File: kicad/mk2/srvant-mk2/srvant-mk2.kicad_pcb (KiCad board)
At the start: 2 copper layers, 172 parts, among them J2 Bus_M.2_Socket_M, J4 ARJM11, J5 ARJM11, U1 INA219AxDCN, U10 RT9742SNGV, U11 BSZ040N04LSGATMA1, U13 KSZ9131RNXI-TR, U14 TPD4EUSB30, U15 TPD4EUSB30, U2 AP64501SP-13, U5 PCF85063AT/AAZ, U6 74LVC1G07SE-7, U7 74LVC1G07SE-7, U8 TPD4EUSB30, U9 TPD4EUSB30, Y1 X32K768S301

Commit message: more progress
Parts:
- removed C30, C31: 100n, Capacitor_SMD:C_0402_1005Metric
- removed R8: 100K/1%, Resistor_SMD:R_0402_1005Metric
- removed U11: BSZ040N04LSGATMA1, footprints:bsz086p03ns
- removed U12: ~, rp-t113-s3:rp-t113-s3
- added C76: 100n, Capacitor_SMD:C_0402_1005Metric, F.Cu at (38.9, 121.3)
- added FB7: 220R, Resistor_SMD:R_0402_1005Metric, F.Cu at (38.9, 119.3)
- added J1: Barrel_Jack_Switch, footprints:DC-jack-694106301002, F.Cu at (153.2, 82.0)
- added J3: HDMI connector, footprints:HDMI-10029449-001RLF, F.Cu at (148.3, 68.8)
- added Q1: DMP3013SFV-7, Package_SON:Diodes_PowerDI3333-8, F.Cu at (141.4, 90.7)
- added R1: 12K, Resistor_SMD:R_0402_1005Metric, F.Cu at (148.5, 89.3)
- added R15: 3.3K, Resistor_SMD:R_0402_1005Metric, F.Cu at (34.0, 119.3)
- added R16: 3.3K, Resistor_SMD:R_0402_1005Metric, F.Cu at (34.0, 121.3)
- added R17: 10R, Resistor_SMD:R_0402_1005Metric, F.Cu at (34.0, 123.3)
- added R18: 10R, Resistor_SMD:R_0402_1005Metric, F.Cu at (34.0, 125.3)
- added TP1: TestPoint (VIN), TestPoint:TestPoint_Pad_D1.0mm, F.Cu at (145.5, 89.8)
- added U3: TLV62585DRLR, TLV62585DRLR:DRL0006A, F.Cu at (43.9, 119.9)
- added U4: rp-t113-s3, rp-t113-s3:rp-t113-s3, F.Cu at (12.8, 38.6)
- added Y2: 25Mhz, footprints:LFXTAL-25MHz, F.Cu at (161.9, 80.0)
- TP8: footprint TestPoint:TestPoint_Pad_2.0x2.0mm -> TestPoint:TestPoint_Pad_D1.0mm
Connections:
- J4 pad SH: GND -> Net-(FB7-Pad1)
- TP8 pad 1: Net-(D2-K) -> /bmc/PHY_DVDDH
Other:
- board outline added: 5.8 x 5.9 mm

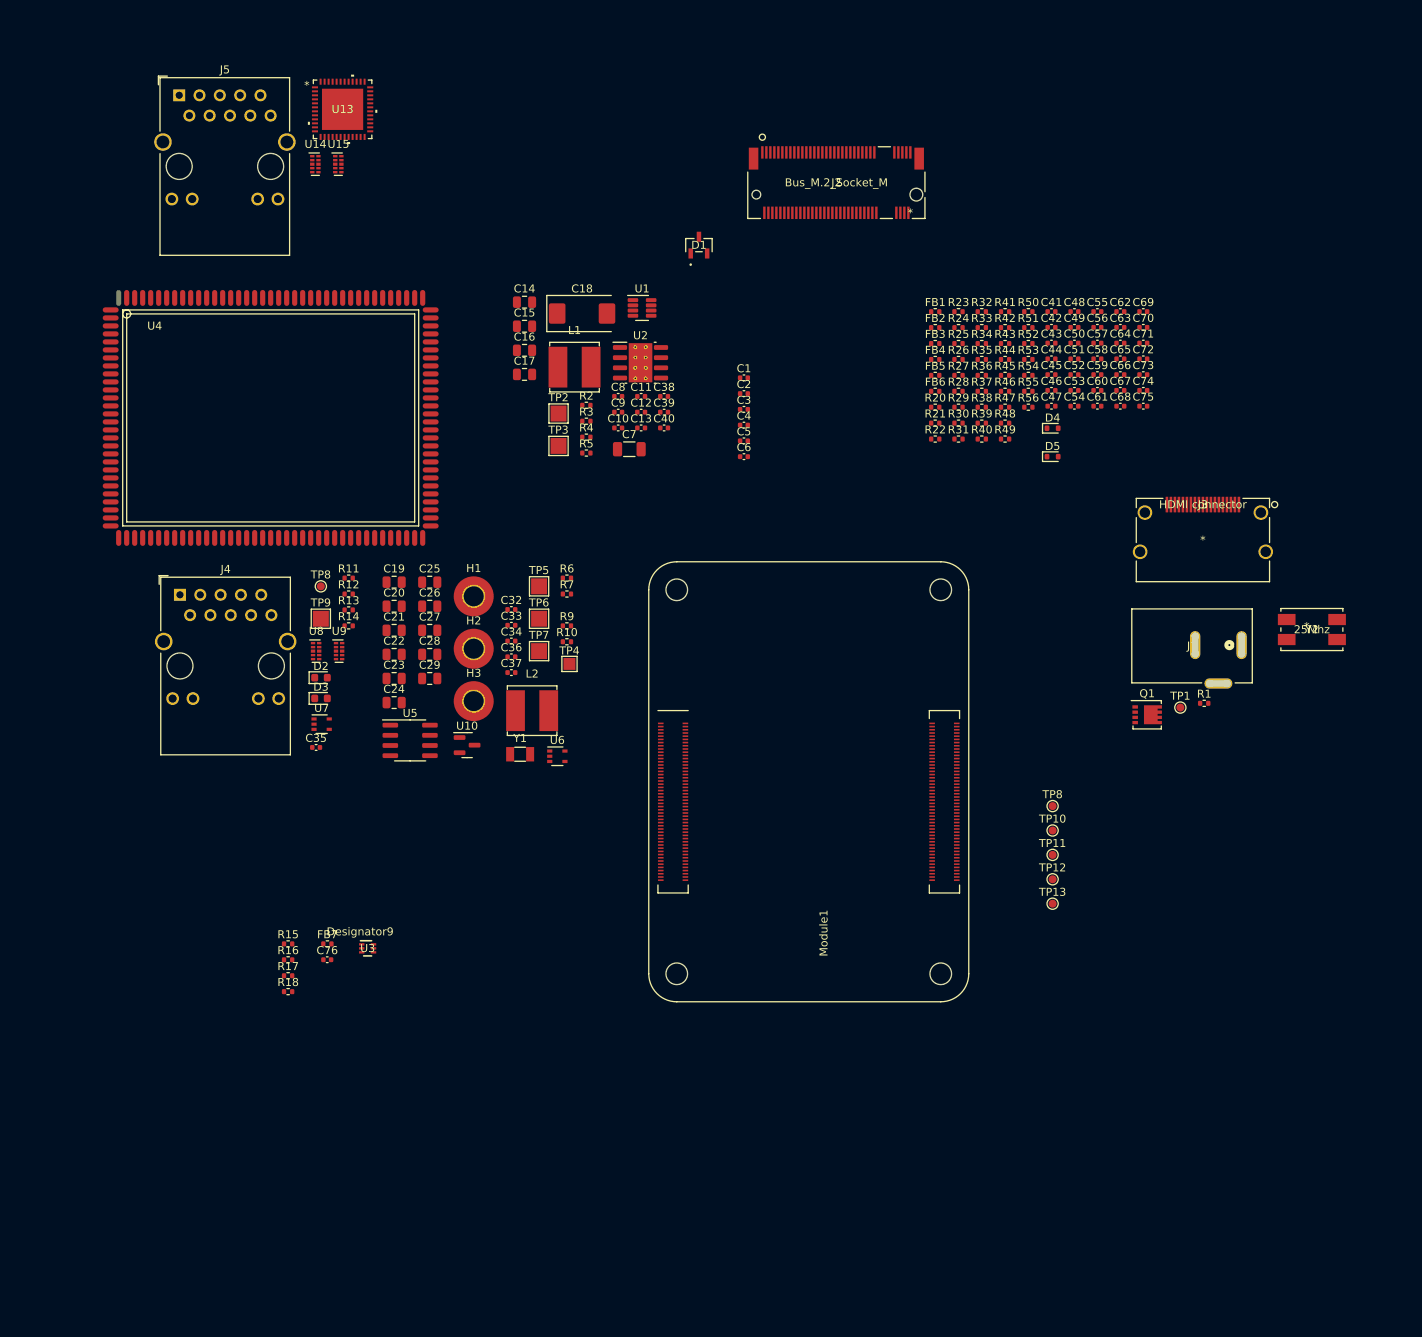
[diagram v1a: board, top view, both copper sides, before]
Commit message: merge cm4 into one page, basic interconnection
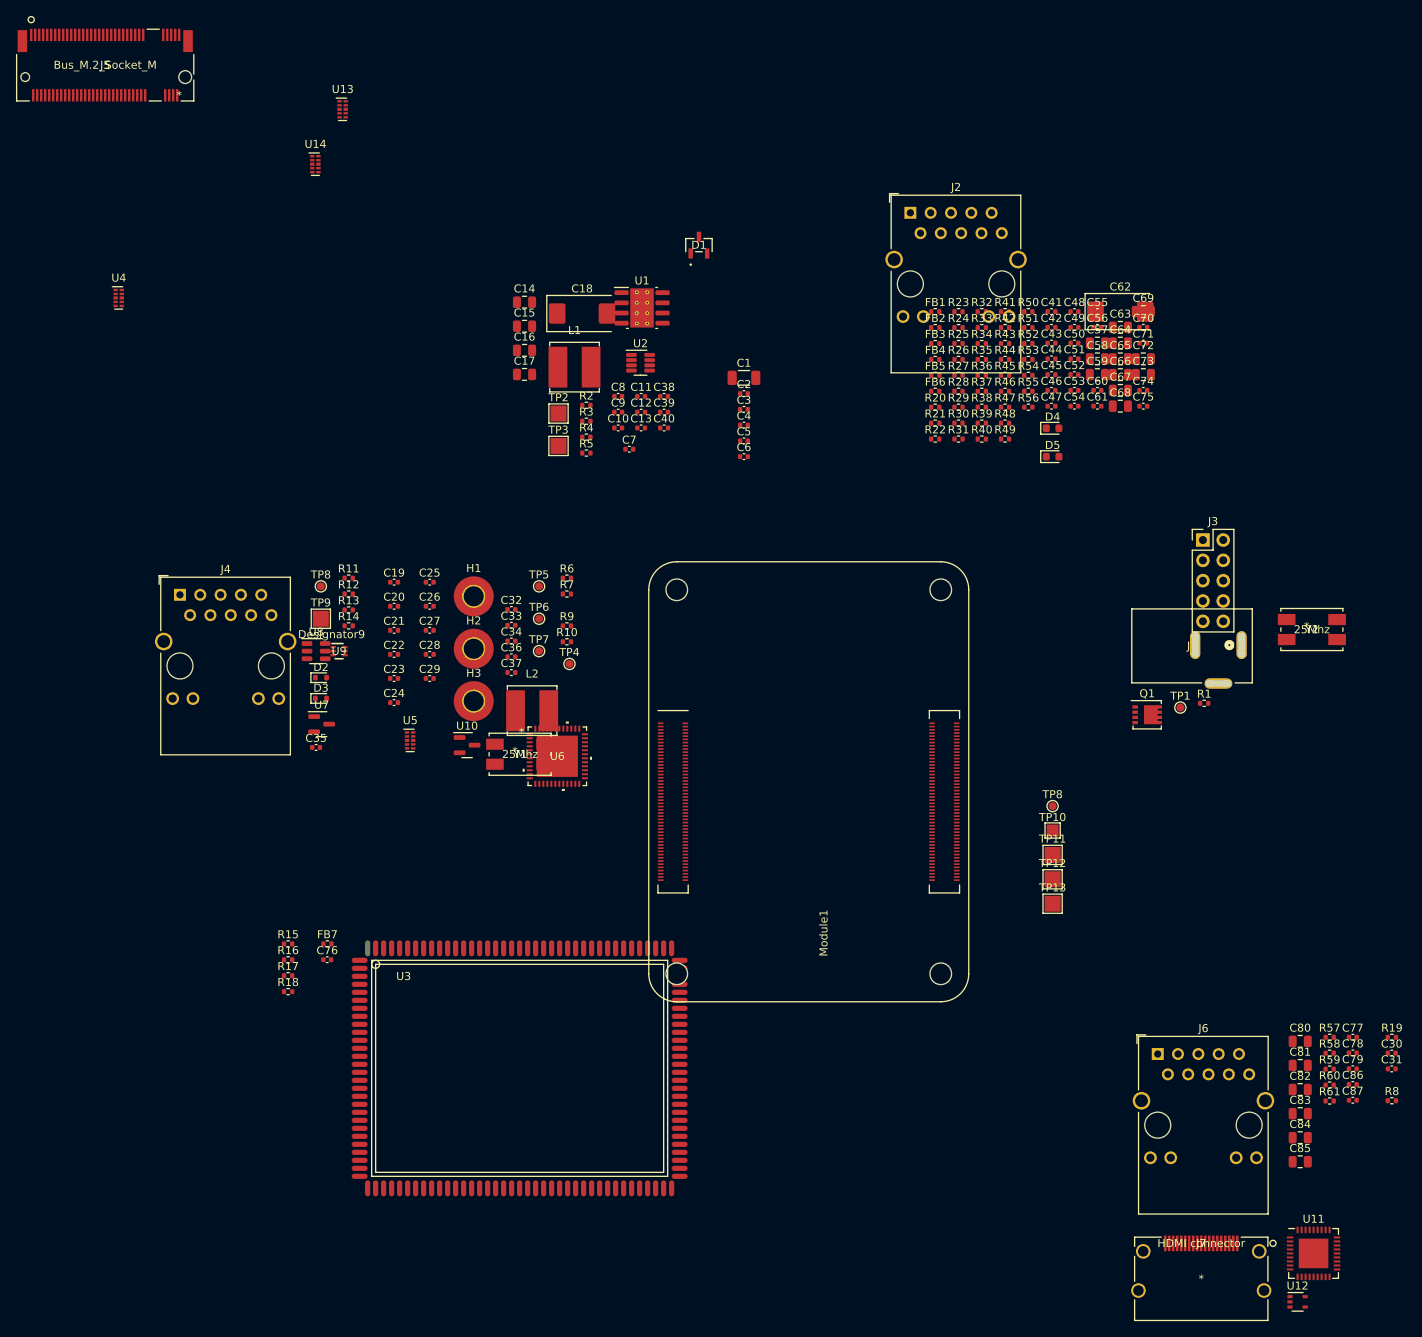
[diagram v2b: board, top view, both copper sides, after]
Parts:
- removed U15: TPD4EUSB30, Package_SON:USON-10_2.5x1.0mm_P0.5mm
- added C30: 100n, Capacitor_SMD:C_0402_1005Metric, F.Cu at (171.9, 133.0)
- added C31: 100n, Capacitor_SMD:C_0402_1005Metric, F.Cu at (171.9, 134.9)
- added C77: 100n, Capacitor_SMD:C_0402_1005Metric, F.Cu at (167.1, 131.0)
- added C78: 100n, Capacitor_SMD:C_0402_1005Metric, F.Cu at (167.1, 133.0)
- added C79: 100n, Capacitor_SMD:C_0402_1005Metric, F.Cu at (167.1, 134.9)
- added C80: 10u, Capacitor_SMD:C_0805_2012Metric, F.Cu at (160.5, 131.5)
- added C81: 10u, Capacitor_SMD:C_0805_2012Metric, F.Cu at (160.5, 134.5)
- added C82: 10u, Capacitor_SMD:C_0805_2012Metric, F.Cu at (160.5, 137.5)
- added C83: 100n, Capacitor_SMD:C_0805_2012Metric, F.Cu at (160.5, 140.5)
- added C84: 100n, Capacitor_SMD:C_0805_2012Metric, F.Cu at (160.5, 143.6)
- added C85: 100n, Capacitor_SMD:C_0805_2012Metric, F.Cu at (160.5, 146.6)
- added C86: 100n, Capacitor_SMD:C_0402_1005Metric, F.Cu at (167.1, 136.9)
- added C87: 100n, Capacitor_SMD:C_0402_1005Metric, F.Cu at (167.1, 138.9)
- added J6: ARJM11, Connector_RJ:RJ45_Wuerth_7499111446_Horizontal, F.Cu at (142.7, 133.1)
- added J7: HDMI connector, footprints:HDMI-10029449-001RLF, F.Cu at (148.1, 161.2)
- added R19: 10K, Resistor_SMD:R_0402_1005Metric, F.Cu at (172.0, 131.0)
- added R57: 12K/1%, Resistor_SMD:R_0402_1005Metric, F.Cu at (164.2, 131.0)
- added R58: 36K/1%, Resistor_SMD:R_0402_1005Metric, F.Cu at (164.2, 133.0)
- added R59: 1K, Resistor_SMD:R_0402_1005Metric, F.Cu at (164.2, 135.0)
- added R60: 470R, Resistor_SMD:R_0402_1005Metric, F.Cu at (164.2, 137.0)
- added R61: 470R, Resistor_SMD:R_0402_1005Metric, F.Cu at (164.2, 139.0)
- added R8: 10R, Resistor_SMD:R_0402_1005Metric, F.Cu at (172.0, 138.9)
- added U11: USB2514B-I/M2, Package_DFN_QFN:QFN-36-1EP_6x6mm_P0.5mm_EP3.7x3.7mm, F.Cu at (162.2, 158.0)
- added U12: 74LVC1G07SE-7, Package_TO_SOT_SMD:SOT-353_SC-70-5, F.Cu at (160.2, 164.1)
- C1: value 10u/35v -> 100n/100v; footprint Capacitor_SMD:C_0402_1005Metric -> Capacitor_SMD:C_1206_3216Metric
- C19: value 10u 35v -> 100n; footprint Capacitor_SMD:C_0805_2012Metric -> Capacitor_SMD:C_0402_1005Metric
- C2, C39, C75: value 10u/35v -> 100n
- C20: value 10u 35v -> 10u/35v; footprint Capacitor_SMD:C_0805_2012Metric -> Capacitor_SMD:C_0402_1005Metric
- C21, C24, C25, C26, C28: value 10u -> 100n; footprint Capacitor_SMD:C_0805_2012Metric -> Capacitor_SMD:C_0402_1005Metric
- C22: value 10u -> 10u/35v; footprint Capacitor_SMD:C_0805_2012Metric -> Capacitor_SMD:C_0402_1005Metric
- C23, C27, C29: footprint Capacitor_SMD:C_0805_2012Metric -> Capacitor_SMD:C_0402_1005Metric
- C37, C41, C42, C43, C44, C8, C9: value 100n -> 10u/35v
- C55, C56: value 100n -> 15p
- C57, C59: value 100n -> 10u 35v; footprint Capacitor_SMD:C_0402_1005Metric -> Capacitor_SMD:C_0805_2012Metric
- C58, C63, C69: value 100n -> 10u; footprint Capacitor_SMD:C_0402_1005Metric -> Capacitor_SMD:C_0805_2012Metric
- C62: value 100n -> 100u; footprint Capacitor_SMD:C_0402_1005Metric -> Capacitor_Tantalum_SMD:CP_EIA-7343-31_Kemet-D
- C64, C65, C66, C67, C68, C73: value 10u/35v -> 10u; footprint Capacitor_SMD:C_0402_1005Metric -> Capacitor_SMD:C_0805_2012Metric
- C7: value 100n/100v -> 10u/35v; footprint Capacitor_SMD:C_1206_3216Metric -> Capacitor_SMD:C_0402_1005Metric
- C70: value 100n -> 27p
- C71: value 15p -> 27p
- C72: value 15p -> 10u; footprint Capacitor_SMD:C_0402_1005Metric -> Capacitor_SMD:C_0805_2012Metric
- D2: value LED Green -> 1N4148; footprint LED_SMD:LED_0603_1608Metric -> Diode_SMD:D_SOD-523
- D3: value LED Red -> 1N4148; footprint LED_SMD:LED_0603_1608Metric -> Diode_SMD:D_SOD-523
- D4: value 1N4148 -> LED Green; footprint Diode_SMD:D_SOD-523 -> LED_SMD:LED_0603_1608Metric
- D5: value 1N4148 -> LED Red; footprint Diode_SMD:D_SOD-523 -> LED_SMD:LED_0603_1608Metric
- J2: value Bus_M.2_Socket_M -> ARJM11; footprint footprints:1-2199230-5 -> Connector_RJ:RJ45_Wuerth_7499111446_Horizontal
- J3: value HDMI connector -> Conn_02x05_Odd_Even; footprint footprints:HDMI-10029449-001RLF -> Connector_PinHeader_2.54mm:PinHeader_2x05_P2.54mm_Vertical
- J5: value ARJM11 -> Bus_M.2_Socket_M; footprint Connector_RJ:RJ45_Wuerth_7499111446_Horizontal -> footprints:1-2199230-5
- R10, R9: value 510K/1% -> 3.3K
- R11, R12: value 1K -> 330R
- R13, R14: value 470R -> 22R
- R15, R16: value 3.3K -> 22R
- R17, R18: value 10R -> 22R
- R2: value 20K 1% -> 10R
- R20: value 330R -> 10K
- R21: value 330R -> 1K
- R24: value 10K -> 6.04K
- R25: value 6.04K -> 10K
- R26, R28, R30: value 22R -> 1K
- R27, R29, R37: value 22R -> 10K
- R3: value 12K 1% -> 20K 1%
- R38, R40, R47, R54: value 10K -> 1K
- R4: value 2.2K 1% -> 12K 1%
- R44, R46: value 1K -> 10K
- R48: value 1K -> 15K/1%
- R49: value 10K -> 100K 1%
- R5: value 10R -> 2.2K 1%
- R50: value 1K -> 22K 1%
- R51: value 10K -> 2.2K/1%
- R52: value 1K -> 2.2K/1%
- R53, R55: value 1K -> 36K/1%
- R56: value 10K -> 36K/1%
- R7: value 22K 1% -> 10R
- TP10: footprint TestPoint:TestPoint_Pad_D1.0mm -> TestPoint:TestPoint_Pad_1.5x1.5mm
- TP11, TP12, TP13: footprint TestPoint:TestPoint_Pad_D1.0mm -> TestPoint:TestPoint_Pad_2.0x2.0mm
- TP4: footprint TestPoint:TestPoint_Pad_1.5x1.5mm -> TestPoint:TestPoint_Pad_D1.0mm
- TP5, TP6, TP7: footprint TestPoint:TestPoint_Pad_2.0x2.0mm -> TestPoint:TestPoint_Pad_D1.0mm
- U1: value INA219AxDCN -> AP64501SP-13; footprint Package_TO_SOT_SMD:SOT-23-8 -> Package_SO:SOIC-8-1EP_3.9x4.9mm_P1.27mm_EP2.95x4.9mm_Mask2.71x3.4mm_ThermalVias
- U13: value KSZ9131RNXI-TR -> TPD4EUSB30; footprint KSZ9131RNXI-TR:QFN48_NX_MCH -> Package_SON:USON-10_2.5x1.0mm_P0.5mm
- U2: value AP64501SP-13 -> INA219AxDCN; footprint Package_SO:SOIC-8-1EP_3.9x4.9mm_P1.27mm_EP2.95x4.9mm_Mask2.71x3.4mm_ThermalVias -> Package_TO_SOT_SMD:SOT-23-8
- U3: value TLV62585DRLR -> rp-t113-s3; footprint TLV62585DRLR:DRL0006A -> rp-t113-s3:rp-t113-s3
- U4: value rp-t113-s3 -> TPD4EUSB30; footprint rp-t113-s3:rp-t113-s3 -> Package_SON:USON-10_2.5x1.0mm_P0.5mm
- U5: value PCF85063AT/AAZ -> TPD4EUSB30; footprint Package_SO:SOIC-8_3.9x4.9mm_P1.27mm -> Package_SON:USON-10_2.5x1.0mm_P0.5mm
- U6: value 74LVC1G07SE-7 -> KSZ9131RNXI-TR; footprint Package_TO_SOT_SMD:SOT-353_SC-70-5 -> KSZ9131RNXI-TR:QFN48_NX_MCH
- U7: value 74LVC1G07SE-7 -> RT9742SNGV; footprint Package_TO_SOT_SMD:SOT-353_SC-70-5 -> Package_TO_SOT_SMD:SOT-23
- U8: value TPD4EUSB30 -> AP22653W6; footprint Package_SON:USON-10_2.5x1.0mm_P0.5mm -> Package_TO_SOT_SMD:SOT-23-6
- U9: value TPD4EUSB30 -> TLV62585DRLR; footprint Package_SON:USON-10_2.5x1.0mm_P0.5mm -> TLV62585DRLR:DRL0006A
- Y1: value X32K768S301 -> 25Mhz; footprint Crystal:Crystal_SMD_3215-2Pin_3.2x1.5mm -> footprints:LFXTAL-25MHz
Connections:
- net /cm4/CM4_GPIO/+1.8v renamed /cm4/+1.8v
- net /cm4/CM4_GPIO/BT_nDis renamed /cm4/BT_nDis
- net /cm4/CM4_GPIO/EEPROM_nWP renamed /cm4/EEPROM_nWP
- net /cm4/CM4_GPIO/GLOBAL_EN renamed /cm4/GLOBAL_EN
- net /cm4/CM4_GPIO/GPIO10 renamed /cm4/GPIO10
- net /cm4/CM4_GPIO/GPIO11 renamed /cm4/GPIO11
- net /cm4/CM4_GPIO/GPIO12 renamed /cm4/GPIO12
- net /cm4/CM4_GPIO/GPIO13 renamed /cm4/GPIO13
- net /cm4/CM4_GPIO/GPIO16 renamed /cm4/GPIO16
- net /cm4/CM4_GPIO/GPIO17 renamed /cm4/GPIO17
- net /cm4/CM4_GPIO/GPIO18 renamed /cm4/GPIO18
- net /cm4/CM4_GPIO/GPIO19 renamed /cm4/GPIO19
- net /cm4/CM4_GPIO/GPIO2 renamed /cm4/GPIO2
- net /cm4/CM4_GPIO/GPIO20 renamed /cm4/GPIO20
- net /cm4/CM4_GPIO/GPIO21 renamed /cm4/GPIO21
- net /cm4/CM4_GPIO/GPIO22 renamed /cm4/GPIO22
- net /cm4/CM4_GPIO/GPIO23 renamed /cm4/GPIO23
- net /cm4/CM4_GPIO/GPIO24 renamed /cm4/GPIO24
- net /cm4/CM4_GPIO/GPIO25 renamed /cm4/GPIO25
- net /cm4/CM4_GPIO/GPIO26 renamed /cm4/GPIO26
- net /cm4/CM4_GPIO/GPIO27 renamed /cm4/GPIO27
- net /cm4/CM4_GPIO/GPIO3 renamed /cm4/GPIO3
- net /cm4/CM4_GPIO/GPIO4 renamed /cm4/GPIO4
- net /cm4/CM4_GPIO/GPIO5 renamed /cm4/GPIO5
- net /cm4/CM4_GPIO/GPIO6 renamed /cm4/GPIO6
- net /cm4/CM4_GPIO/GPIO7 renamed /cm4/GPIO7
- net /cm4/CM4_GPIO/GPIO8 renamed /cm4/GPIO8
- net /cm4/CM4_GPIO/GPIO9 renamed /cm4/GPIO9
- net /cm4/CM4_GPIO/HOST_RUN_PG renamed /cm4/HOST_RUN_PG
- net /cm4/CM4_GPIO/HOST_nRPIBOOT renamed /cm4/HOST_nRPIBOOT
- net /cm4/CM4_GPIO/ID_SC renamed /cm4/ID_SC
- net /cm4/CM4_GPIO/ID_SD renamed /cm4/ID_SD
- net /cm4/CM4_GPIO/SCL0 renamed /cm4/SCL0
- net /cm4/CM4_GPIO/SDA0 renamed /cm4/SDA0
- net /cm4/CM4_GPIO/SD_CLK renamed /cm4/SD_CLK
- net /cm4/CM4_GPIO/SD_DAT0 renamed /cm4/SD_DAT0
- net /cm4/CM4_GPIO/SD_DAT1 renamed /cm4/SD_DAT1
- net /cm4/CM4_GPIO/SD_DAT2 renamed /cm4/SD_DAT2
- net /cm4/CM4_GPIO/SD_DAT3 renamed /cm4/SD_DAT3
- net /cm4/CM4_GPIO/SD_PWR_ON renamed /cm4/SD_PWR_ON
- net /cm4/CM4_GPIO/SYNC_IN renamed /cm4/SYNC_IN
- net /cm4/CM4_GPIO/SYNC_OUT renamed /cm4/SYNC_OUT
- net /cm4/CM4_GPIO/WL_nDis renamed /cm4/WL_nDis
- net /cm4/cm4-high-speed/CAM0_C_N renamed /cm4/CAM0_C_N
- net /cm4/cm4-high-speed/CAM0_C_P renamed /cm4/CAM0_C_P
- net /cm4/cm4-high-speed/CAM0_D0_N renamed /cm4/CAM0_D0_N
- net /cm4/cm4-high-speed/CAM0_D0_P renamed /cm4/CAM0_D0_P
- net /cm4/cm4-high-speed/CAM0_D1_N renamed /cm4/CAM0_D1_N
- net /cm4/cm4-high-speed/CAM0_D1_P renamed /cm4/CAM0_D1_P
- net /cm4/cm4-high-speed/CAM1_C_N renamed /cm4/CAM1_C_N
- net /cm4/cm4-high-speed/CAM1_C_P renamed /cm4/CAM1_C_P
- net /cm4/cm4-high-speed/CAM1_D0_N renamed /cm4/CAM1_D0_N
- net /cm4/cm4-high-speed/CAM1_D0_P renamed /cm4/CAM1_D0_P
- net /cm4/cm4-high-speed/CAM1_D1_N renamed /cm4/CAM1_D1_N
- net /cm4/cm4-high-speed/CAM1_D1_P renamed /cm4/CAM1_D1_P
- net /cm4/cm4-high-speed/CAM1_D2_N renamed /cm4/CAM1_D2_N
- net /cm4/cm4-high-speed/CAM1_D2_P renamed /cm4/CAM1_D2_P
- net /cm4/cm4-high-speed/CAM1_D3_N renamed /cm4/CAM1_D3_N
- net /cm4/cm4-high-speed/CAM1_D3_P renamed /cm4/CAM1_D3_P
- net /cm4/cm4-high-speed/DSI0_C_N renamed /cm4/DSI0_C_N
- net /cm4/cm4-high-speed/DSI0_C_P renamed /cm4/DSI0_C_P
- net /cm4/cm4-high-speed/DSI0_D0_N renamed /cm4/DSI0_D0_N
- net /cm4/cm4-high-speed/DSI0_D0_P renamed /cm4/DSI0_D0_P
- net /cm4/cm4-high-speed/DSI0_D1_N renamed /cm4/DSI0_D1_N
- net /cm4/cm4-high-speed/DSI0_D1_P renamed /cm4/DSI0_D1_P
- net /cm4/cm4-high-speed/DSI1_C_N renamed /cm4/DSI1_C_N
- net /cm4/cm4-high-speed/DSI1_C_P renamed /cm4/DSI1_C_P
- net /cm4/cm4-high-speed/DSI1_D0_N renamed /cm4/DSI1_D0_N
- net /cm4/cm4-high-speed/DSI1_D0_P renamed /cm4/DSI1_D0_P
- net /cm4/cm4-high-speed/DSI1_D1_N renamed /cm4/DSI1_D1_N
- net /cm4/cm4-high-speed/DSI1_D1_P renamed /cm4/DSI1_D1_P
- net /cm4/cm4-high-speed/DSI1_D2_N renamed /cm4/DSI1_D2_N
- net /cm4/cm4-high-speed/DSI1_D2_P renamed /cm4/DSI1_D2_P
- net /cm4/cm4-high-speed/DSI1_D3_N renamed /cm4/DSI1_D3_N
- net /cm4/cm4-high-speed/DSI1_D3_P renamed /cm4/DSI1_D3_P
- net /cm4/cm4-high-speed/HDMI1_CEC renamed /cm4/HDMI1_CEC
- net /cm4/cm4-high-speed/HDMI1_CK_N renamed /cm4/HDMI1_CK_N
- net /cm4/cm4-high-speed/HDMI1_CK_P renamed /cm4/HDMI1_CK_P
- net /cm4/cm4-high-speed/HDMI1_D0_N renamed /cm4/HDMI1_D0_N
- net /cm4/cm4-high-speed/HDMI1_D0_P renamed /cm4/HDMI1_D0_P
- net /cm4/cm4-high-speed/HDMI1_D1_N renamed /cm4/HDMI1_D1_N
- net /cm4/cm4-high-speed/HDMI1_D1_P renamed /cm4/HDMI1_D1_P
- net /cm4/cm4-high-speed/HDMI1_D2_N renamed /cm4/HDMI1_D2_N
- net /cm4/cm4-high-speed/HDMI1_D2_P renamed /cm4/HDMI1_D2_P
- net /cm4/cm4-high-speed/HDMI1_HOTPLUG renamed /cm4/HDMI1_HOTPLUG
- net /cm4/cm4-high-speed/HDMI1_SCL renamed /cm4/HDMI1_SCL
- net /cm4/cm4-high-speed/HDMI1_SDA renamed /cm4/HDMI1_SDA
- net /cm4/cm4-high-speed/TV_OUT renamed /cm4/TV_OUT
- net /cm4/cm4-high-speed/USB2_N renamed /cm4/USB2_N
- net /cm4/cm4-high-speed/USB2_P renamed /cm4/USB2_P
- net /cm4/cm4-high-speed/USBOTG_ID renamed /cm4/USBOTG_ID
- C1 pad 1: Net-(D1-K) -> Net-(Q1-D)
- C10 pad 1: Net-(D1-K) -> Net-(U1-SS)
- C10 pad 2: Net-(D1-A) -> GND
- C11 pad 1: Net-(U2-COMP) -> Net-(U1-COMP)
- C13 pad 2: Net-(U2-FB) -> Net-(U1-FB)
- C14 pad 1: /power/+5v -> /bmc/+5v
- C15 pad 1: /power/+5v -> /bmc/+5v
- C16 pad 1: /power/+5v -> /bmc/+5v
- C17 pad 1: /power/+5v -> /bmc/+5v
- C18 pad 1: /power/+5v -> /bmc/+5v
- C19 pad 1: /cm4/cm4-high-speed/+5v -> Net-(U2-IN+)
- C19 pad 2: GND -> Net-(U2-IN-)
- C2 pad 2: GND -> Net-(D1-A)
- C20 pad 1: /cm4/cm4-high-speed/+5v -> /bmc/3.3v
- C21 pad 1: /cm4/cm4-high-speed/+3V3 PCIe -> /bmc/3.3v
- C22 pad 1: /cm4/cm4-high-speed/+3V3 PCIe -> /bmc/PHY_DVDDL
- C23 pad 1: /cm4/cm4-high-speed/+3V3 PCIe -> /bmc/PHY_DVDDL
- C24 pad 1: /cm4/cm4-high-speed/+3V3 PCIe -> /bmc/PHY_DVDDL
- C25 pad 1: /cm4/cm4-high-speed/+3V3 PCIe -> /bmc/PHY_DVDDL
- C26 pad 1: /cm4/cm4-high-speed/+3V3 PCIe -> /bmc/PHY_AVDDL_PLL
- C27 pad 1: /cm4/cm4-high-speed/+3V3 PCIe -> /bmc/PHY_DVDDL
- C28 pad 1: /cm4/cm4-high-speed/+3V3 PCIe -> Net-(C28-Pad1)
- C29 pad 1: /cm4/cm4-high-speed/+3V3 PCIe -> /bmc/PHY_AVDDL
- C32 pad 1: /cm4/cm4-high-speed/+5v -> Net-(C32-Pad1)
- C33 pad 1: /cm4/cm4-high-speed/+BATT -> /bmc/PHY_AVDDL
- C34 pad 1: Net-(C34-Pad1) -> /bmc/PHY_AVDDL_PLL
- C34 pad 2: /cm4/cm4-high-speed/nRTC_INT -> GND
- C35 pad 1: Net-(C35-Pad1) -> /bmc/PHY_DVDDL
- C36 pad 1: /cm4/cm4-high-speed/+5v -> /bmc/PHY_AVDDL
- C37 pad 1: /cm4/cm4-high-speed/HDMI_5v -> /bmc/PHY_AVDDL_PLL
- C38 pad 1: /power/+3.3v -> /bmc/PHY_DVDDL
- C39 pad 1: Net-(D1-K) -> /bmc/PHY_AVDDL
- C40 pad 1: /power/+3.3v -> /bmc/PHY_AVDDL
- C41 pad 1: /bmc/PHY_DVDDH -> /bmc/PHY_RESET_N
- C42 pad 1: /bmc/PHY_DVDDH -> /bmc/PHY_AVDDH
- C43 pad 1: /bmc/PHY_DVDDH -> /bmc/1V2
- C45 pad 1: /bmc/PHY_DVDDH -> /bmc/PHY_AVDDH
- C46 pad 1: /bmc/PHY_AVDDH -> /bmc/1V2
- C47 pad 1: /bmc/PHY_AVDDH -> /bmc/PHY_DVDDH
- C49 pad 1: /bmc/PHY_AVDDH -> /bmc/PHY_DVDDH
- C50 pad 1: /bmc/PHY_AVDDL -> /bmc/PHY_AVDDH
- C51 pad 1: /bmc/PHY_AVDDL -> /bmc/PHY_DVDDH
- C52 pad 1: /bmc/PHY_AVDDL -> /bmc/PHY_AVDDH
- C53 pad 1: /bmc/PHY_AVDDL -> /bmc/PHY_DVDDH
- C54 pad 1: /bmc/PHY_AVDDL_PLL -> /bmc/PHY_DVDDH
- C55 pad 1: /bmc/PHY_AVDDL_PLL -> GND
- C55 pad 2: GND -> Net-(U6-XI)
- C56 pad 1: /bmc/PHY_AVDDL_PLL -> Net-(U6-XO)
- C57 pad 1: /bmc/PHY_DVDDL -> /bmc/+5v
- C58 pad 1: /bmc/PHY_DVDDL -> /bmc/+5v
- C59 pad 1: /bmc/PHY_DVDDL -> /bmc/+5v
- C60 pad 1: /bmc/PHY_DVDDL -> /bmc/+5v
- C61 pad 1: /bmc/PHY_DVDDL -> /cm4/HDMI_5v
- C62 pad 1: /bmc/PHY_DVDDL -> /cm4/VBUS
- C63 pad 1: /bmc/PHY_DVDDL -> /cm4/VBUS
- C64 pad 1: /bmc/PHY_AVDDH -> /cm4/VBUS
- C65 pad 1: /bmc/PHY_DVDDH -> /cm4/+3V3 PCIe
- C66 pad 1: /bmc/PHY_AVDDL -> /cm4/VBUS
- C67 pad 1: /bmc/PHY_AVDDL_PLL -> /cm4/+3V3 PCIe
- C68 pad 1: /bmc/PHY_DVDDL -> /cm4/VBUS
- C69 pad 1: Net-(C69-Pad1) -> /cm4/+3V3 PCIe
- C7 pad 1: Net-(Q1-D) -> Net-(D1-K)
- C70 pad 1: Net-(C70-Pad1) -> /cm4/XTALIN
- C71 pad 1: Net-(U13-XO) -> /cm4/XTALOUT
- C72 pad 1: GND -> /cm4/+3.3v
- C72 pad 2: Net-(U13-XI) -> GND
- C73 pad 1: /bmc/1V2 -> /cm4/+3.3v
- C74 pad 1: /bmc/1V2 -> /cm4/+3.3v
- C75 pad 1: /bmc/PHY_RESET_N -> /cm4/+3.3v
- C76 pad 1: Net-(C35-Pad1) -> /cm4/+3.3v
- C8 pad 1: Net-(U1-IN+) -> Net-(D1-K)
- C8 pad 2: Net-(U1-IN-) -> GND
- C9 pad 1: Net-(U2-SS) -> Net-(D1-K)
- D2 pad 1: Net-(D2-K) -> /bmc/PHY_DVDDH
- D2 pad 2: /cm4/CM4_GPIO/+3.3v -> /bmc/PHY_RESET_N
- D3 pad 1: Net-(D3-K) -> /bmc/RESET_OUT_N
- D3 pad 2: /cm4/CM4_GPIO/+3.3v -> /bmc/PHY_RESET_N
- D4 pad 1: /bmc/PHY_DVDDH -> Net-(D4-K)
- D4 pad 2: /bmc/PHY_RESET_N -> /cm4/+3.3v
- D5 pad 1: /bmc/RESET_OUT_N -> Net-(D5-K)
- D5 pad 2: /bmc/PHY_RESET_N -> /cm4/+3.3v
- FB1 pad 2: /bmc/PHY_AVDDL -> /bmc/PHY_DVDDL
- FB3 pad 2: /bmc/PHY_DVDDL -> /bmc/PHY_AVDDL
- FB4 pad 1: /bmc/PHY_AVDDH -> GND
- FB4 pad 2: /bmc/3.3v -> Net-(FB4-Pad2)
- FB5 pad 1: /bmc/PHY_DVDDH -> /bmc/PHY_AVDDH
- FB6 pad 1: GND -> /bmc/PHY_DVDDH
- FB6 pad 2: Net-(FB6-Pad2) -> /bmc/3.3v
- J2 pad 1: GND -> /bmc/TXRXA_P
- J2 pad 10: unconnected-(J2-DAS/~DSS~/~LED1-Pad10) -> /bmc/TXRXD_N
- J2 pad 11: unconnected-(J2-PETn3-Pad11) -> /bmc/PHY_DVDDH
- J2 pad 12: /cm4/cm4-high-speed/+3V3 PCIe -> Net-(J2-LED2-)
- J2 pad 13: unconnected-(J2-PETp3-Pad13) -> /bmc/PHY_DVDDH
- J2 pad 14: /cm4/cm4-high-speed/+3V3 PCIe -> Net-(J2-LED1-)
- J2 pad 2: /cm4/cm4-high-speed/+3V3 PCIe -> /bmc/TXRXA_N
- J2 pad 3: GND -> /bmc/TXRXB_P
- J2 pad 4: /cm4/cm4-high-speed/+3V3 PCIe -> /bmc/TXRXB_N
- J2 pad 5: unconnected-(J2-PERn3-Pad5) -> Net-(C28-Pad1)
- J2 pad 6: unconnected-(J2-NC-Pad6) -> Net-(C32-Pad1)
- J2 pad 7: unconnected-(J2-PERp3-Pad7) -> /bmc/TXRXC_P
- J2 pad 8: unconnected-(J2-NC-Pad8) -> /bmc/TXRXC_N
- J2 pad 9: GND -> /bmc/TXRXD_P
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
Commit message: more progress
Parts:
- removed R57: 12K/1%, Resistor_SMD:R_0402_1005Metric
- removed the TP8 at (129.5, 102.1)
- removed the TP8 at (38.1, 74.6)
- added BT1: Battery_Cell, footprints:battery-S8411-45R, F.Cu at (81.3, 59.0)
- added C100: 10u, Capacitor_SMD:C_0805_2012Metric, F.Cu at (-49.3, 13.0)
- added C101: 100n, Capacitor_SMD:C_0805_2012Metric, F.Cu at (-49.3, 16.1)
- added C102: 100n, Capacitor_SMD:C_0805_2012Metric, F.Cu at (-49.3, 19.1)
- added C103: 100n, Capacitor_SMD:C_0805_2012Metric, F.Cu at (-49.3, 22.1)
- added C104: 100n, Capacitor_SMD:C_0402_1005Metric, F.Cu at (-16.3, 30.3)
- added C105: 100n, Capacitor_SMD:C_0402_1005Metric, F.Cu at (-16.3, 32.3)
- added C88: 27p, Capacitor_SMD:C_0402_1005Metric, F.Cu at (-19.2, 24.4)
- added C89: 27p, Capacitor_SMD:C_0402_1005Metric, F.Cu at (-19.2, 26.3)
- added C90: 10u, Capacitor_SMD:C_0805_2012Metric, F.Cu at (-49.3, 1.00)
- added C91: 10u, Capacitor_SMD:C_0805_2012Metric, F.Cu at (-49.3, 4.01)
- added C92: 100n, Capacitor_SMD:C_0402_1005Metric, F.Cu at (-19.2, 28.3)
- added C93: 100n, Capacitor_SMD:C_0402_1005Metric, F.Cu at (-19.2, 30.3)
- added C94: 100n, Capacitor_SMD:C_0402_1005Metric, F.Cu at (-19.2, 32.3)
- added C95: 100n, Capacitor_SMD:C_0402_1005Metric, F.Cu at (-16.3, 24.4)
- added C96: 100n, Capacitor_SMD:C_0402_1005Metric, F.Cu at (-16.3, 26.3)
- added C97: 100n, Capacitor_SMD:C_0402_1005Metric, F.Cu at (-16.3, 28.3)
- added C98: 10u, Capacitor_SMD:C_0805_2012Metric, F.Cu at (-49.3, 7.03)
- added C99: 10u, Capacitor_SMD:C_0805_2012Metric, F.Cu at (-49.3, 10.0)
- added D6: 1N4148, Diode_SMD:D_SOD-523, F.Cu at (-3.99, 0.72)
- added D7: LED Green, LED_SMD:LED_0603_1608Metric, F.Cu at (-12.8, 28.7)
- added D8: LED Red, LED_SMD:LED_0603_1608Metric, F.Cu at (-12.8, 31.3)
- added FB8: 220R, Resistor_SMD:R_0402_1005Metric, F.Cu at (-22.1, 24.4)
- added J10: HDMI connector, footprints:HDMI-10029449-001RLF, F.Cu at (63.1, 192.4)
- added J8: Bus_M.2_Socket_M, footprints:1-2199230-5, F.Cu at (93.3, 157.4)
- added J9: ARJM11, Connector_RJ:RJ45_Wuerth_7499111446_Horizontal, F.Cu at (79.1, 177.5)
- added L3: SRN6045TA-3R3Y, Inductor_SMD:L_Bourns_SRN6045TA, F.Cu at (76.7, 167.6)
- added R62: 36K/1%, Resistor_SMD:R_0402_1005Metric, F.Cu at (-22.1, 26.4)
- added R63: 12K/1%, Resistor_SMD:R_0402_1005Metric, F.Cu at (-22.1, 28.4)
- added R64: 36K/1%, Resistor_SMD:R_0402_1005Metric, F.Cu at (-22.1, 30.4)
- added R65: 1K, Resistor_SMD:R_0402_1005Metric, F.Cu at (-22.1, 32.3)
- added R66: 470R, Resistor_SMD:R_0402_1005Metric, F.Cu at (-22.1, 34.3)
- added R67: 470R, Resistor_SMD:R_0402_1005Metric, F.Cu at (-22.1, 36.3)
- added SW1: SW_DIP_x04, DIP_SWITCH_DS04-254-2-04BK-SMT:DS04-254-2-04BK-SMT_CUD, F.Cu at (79.4, 29.2)
- added TP14: TestPoint, TestPoint:TestPoint_Pad_2.0x2.0mm, F.Cu at (1.02, 1.02)
- added TP15: TestPoint, TestPoint:TestPoint_Pad_2.0x2.0mm, F.Cu at (-36.7, 37.4)
- added TP8: TestPoint, TestPoint:TestPoint_Pad_D1.0mm, F.Cu at (-4.29, 3.48)
- added U15: TLV62585DRLR, TLV62585DRLR:DRL0006A, F.Cu at (83.1, 165.6)
- added U16: FSUSB42MUX, footprints:FSUSB42UMX, F.Cu at (43.4, 163.2)
- added U17: USB2514B-I/M2, Package_DFN_QFN:QFN-36-1EP_6x6mm_P0.5mm_EP3.7x3.7mm, F.Cu at (43.6, 171.7)
- added U18: 74LVC1G07SE-7, Package_TO_SOT_SMD:SOT-353_SC-70-5, F.Cu at (-37.1, 47.6)
- added U19: TPD4EUSB30, Package_SON:USON-10_2.5x1.0mm_P0.5mm, F.Cu at (-13.4, 25.4)
- added U20: TPD4EUSB30, Package_SON:USON-10_2.5x1.0mm_P0.5mm, F.Cu at (-10.6, 25.4)
- added Y3: 24MHz, footprints:LFXTAL-25MHz, F.Cu at (-15.8, 36.5)
- C10, C30, C60, C61: value 100n -> 10u/35v
- C11, C13: value 220pF -> 10u/35v
- C12: value 1.2nF -> 10u/35v
- C14, C15, C63, C64, C65, C66, C67, C68, C69, C72: value 10u -> 100n; footprint Capacitor_SMD:C_0805_2012Metric -> Capacitor_SMD:C_0402_1005Metric
- C16: value 10u -> 220pF; footprint Capacitor_SMD:C_0805_2012Metric -> Capacitor_SMD:C_0402_1005Metric
- C17: value 10u -> 1.2nF; footprint Capacitor_SMD:C_0805_2012Metric -> Capacitor_SMD:C_0402_1005Metric
- C18: value 100uF -> 10u; footprint Capacitor_Tantalum_SMD:CP_EIA-7343-31_Kemet-D -> Capacitor_SMD:C_0805_2012Metric
- C19, C21, C23, C25, C26, C27, C33, C35, C36, C38, C39, C76, C86, C87: value 100n -> 10u; footprint Capacitor_SMD:C_0402_1005Metric -> Capacitor_SMD:C_0805_2012Metric
- C20: value 10u/35v -> 220pF
- C22: value 10u/35v -> 10u; footprint Capacitor_SMD:C_0402_1005Metric -> Capacitor_SMD:C_0805_2012Metric
- C24, C28: value 100n -> 100uF; footprint Capacitor_SMD:C_0402_1005Metric -> Capacitor_Tantalum_SMD:CP_EIA-7343-31_Kemet-D
- C34: value 100n -> 100u; footprint Capacitor_SMD:C_0402_1005Metric -> Capacitor_Tantalum_SMD:CP_EIA-7343-31_Kemet-D
- C37, C41, C42, C43, C44: value 10u/35v -> 100n
- C55: value 15p -> 10u/35v
- C56: value 15p -> 100n
- C57: value 10u 35v -> 100n; footprint Capacitor_SMD:C_0805_2012Metric -> Capacitor_SMD:C_0402_1005Metric
- C58: value 10u -> 10u/35v; footprint Capacitor_SMD:C_0805_2012Metric -> Capacitor_SMD:C_0402_1005Metric
- C59: value 10u 35v -> 10u/35v; footprint Capacitor_SMD:C_0805_2012Metric -> Capacitor_SMD:C_0402_1005Metric
- C62: value 100u -> 10u/35v; footprint Capacitor_Tantalum_SMD:CP_EIA-7343-31_Kemet-D -> Capacitor_SMD:C_0402_1005Metric
- C70, C71: value 27p -> 100n
- C73: value 10u -> 15p; footprint Capacitor_SMD:C_0805_2012Metric -> Capacitor_SMD:C_0402_1005Metric
- C74: value 100n -> 15p
- C75, C77: value 100n -> 10u 35v; footprint Capacitor_SMD:C_0402_1005Metric -> Capacitor_SMD:C_0805_2012Metric
- C80: value 10u -> 100u; footprint Capacitor_SMD:C_0805_2012Metric -> Capacitor_Tantalum_SMD:CP_EIA-7343-31_Kemet-D
- C83, C84, C85: value 100n -> 10u
- D2: value 1N4148 -> BAT54C-7-F; footprint Diode_SMD:D_SOD-523 -> Package_TO_SOT_SMD:SOT-23
- D3: value 1N4148 -> LED; footprint Diode_SMD:D_SOD-523 -> LED_SMD:LED_0603_1608Metric
- D4: value LED Green -> LED
- D5: value LED Red -> 1N4148; footprint LED_SMD:LED_0603_1608Metric -> Diode_SMD:D_SOD-523
- J2: value ARJM11 -> Conn_01x02; footprint Connector_RJ:RJ45_Wuerth_7499111446_Horizontal -> Connector_PinHeader_1.00mm:PinHeader_1x02_P1.00mm_Vertical
- J3: value Conn_02x05_Odd_Even -> Conn_01x03; footprint Connector_PinHeader_2.54mm:PinHeader_2x05_P2.54mm_Vertical -> Connector_PinHeader_2.54mm:PinHeader_1x03_P2.54mm_Vertical
- J4: value ARJM11 -> USB_OTG; footprint Connector_RJ:RJ45_Wuerth_7499111446_Horizontal -> Connector_USB:USB_Micro-B_Amphenol_10103594-0001LF_Horizontal
- J5: value Bus_M.2_Socket_M -> ARJM11; footprint footprints:1-2199230-5 -> Connector_RJ:RJ45_Wuerth_7499111446_Horizontal
- J6: value ARJM11 -> Conn_02x05_Odd_Even; footprint Connector_RJ:RJ45_Wuerth_7499111446_Horizontal -> Connector_PinHeader_2.54mm:PinHeader_2x05_P2.54mm_Vertical
- J7: value HDMI connector -> USB[690-008-221-904]; footprint footprints:HDMI-10029449-001RLF -> footprints:MOLEX_USB_67298-4090
- L1: value SRN6045TA-3R3Y -> SRN4018-4R7M; footprint Inductor_SMD:L_Bourns_SRN6045TA -> Inductor_SMD:L_Bourns-SRN4018
- R11, R12: value 330R -> 3.3K
- R13, R14, R32, R34, R36: value 22R -> 1K
- R15: value 22R -> 15K/1%
- R16: value 22R -> 47K
- R17, R18: value 22R -> 330R
- R19, R20, R22, R37, R39, R41: value 10K -> 22R
- R2: value 10R -> 0.005R; footprint Resistor_SMD:R_0402_1005Metric -> Resistor_SMD:R_0805_2012Metric
- R21, R23, R38, R40, R42: value 1K -> 22R
- R24: value 6.04K -> 22R
- R26, R28, R43, R45, R47: value 1K -> 10K
- R27, R29, R44, R46: value 10K -> 1K
- R3: value 20K 1% -> 10R
- R30: value 1K -> 6.04K
- R31, R33, R35: value 22R -> 10K
- R4: value 12K 1% -> 20K 1%
- R48: value 15K/1% -> 1K
- R49: value 100K 1% -> 1K
- R5: value 2.2K 1% -> 12K 1%
- R50: value 22K 1% -> 10K
- R51: value 2.2K/1% -> 1K
- R52: value 2.2K/1% -> 10K
- R53: value 36K/1% -> 1K
- R54: value 1K -> 15K/1%
- R55: value 36K/1% -> 100K 1%
- R56: value 36K/1% -> 22K 1%
- R58: value 36K/1% -> 2.2K/1%
- R59: value 1K -> 36K/1%
- R6: value 100K 1% -> 2.2K 1%
- R60: value 470R -> 1K
- R61: value 470R -> 36K/1%
- TP10: footprint TestPoint:TestPoint_Pad_1.5x1.5mm -> TestPoint:TestPoint_Pad_D1.0mm
- TP12: footprint TestPoint:TestPoint_Pad_2.0x2.0mm -> TestPoint:TestPoint_Pad_1.5x1.5mm
- TP4, TP5: footprint TestPoint:TestPoint_Pad_D1.0mm -> TestPoint:TestPoint_Pad_2.0x2.0mm
- TP9: footprint TestPoint:TestPoint_Pad_2.0x2.0mm -> TestPoint:TestPoint_Pad_D1.0mm
- U1: value AP64501SP-13 -> AP63205WU; footprint Package_SO:SOIC-8-1EP_3.9x4.9mm_P1.27mm_EP2.95x4.9mm_Mask2.71x3.4mm_ThermalVias -> Package_TO_SOT_SMD:TSOT-23-6
- U10, U7: value RT9742SNGV -> TPD4EUSB30; footprint Package_TO_SOT_SMD:SOT-23 -> Package_SON:USON-10_2.5x1.0mm_P0.5mm
- U11: value USB2514B-I/M2 -> TPD4EUSB30; footprint Package_DFN_QFN:QFN-36-1EP_6x6mm_P0.5mm_EP3.7x3.7mm -> Package_SON:USON-10_2.5x1.0mm_P0.5mm
- U12: value 74LVC1G07SE-7 -> KSZ9131RNXI-TR; footprint Package_TO_SOT_SMD:SOT-353_SC-70-5 -> KSZ9131RNXI-TR:QFN48_NX_MCH
- U13: value TPD4EUSB30 -> RT9742SNGV; footprint Package_SON:USON-10_2.5x1.0mm_P0.5mm -> Package_TO_SOT_SMD:SOT-23
- U14: value TPD4EUSB30 -> AP22653W6; footprint Package_SON:USON-10_2.5x1.0mm_P0.5mm -> Package_TO_SOT_SMD:SOT-23-6
- U2: value INA219AxDCN -> AP64501SP-13; footprint Package_TO_SOT_SMD:SOT-23-8 -> Package_SO:SOIC-8-1EP_3.9x4.9mm_P1.27mm_EP2.95x4.9mm_Mask2.71x3.4mm_ThermalVias
- U3: value rp-t113-s3 -> 74AHC1G32; footprint rp-t113-s3:rp-t113-s3 -> Package_TO_SOT_SMD:SOT-23-5
- U4: value TPD4EUSB30 -> INA219AxDCN; footprint Package_SON:USON-10_2.5x1.0mm_P0.5mm -> Package_TO_SOT_SMD:SOT-23-8
- U5: value TPD4EUSB30 -> rp-t113-s3; footprint Package_SON:USON-10_2.5x1.0mm_P0.5mm -> rp-t113-s3:rp-t113-s3
- U6: value KSZ9131RNXI-TR -> PCF85063AT/AAZ; footprint KSZ9131RNXI-TR:QFN48_NX_MCH -> Package_SO:SOIC-8_3.9x4.9mm_P1.27mm
- U8: value AP22653W6 -> 74LVC2G07
- U9: value TLV62585DRLR -> AP22653W6; footprint TLV62585DRLR:DRL0006A -> Package_TO_SOT_SMD:SOT-23-6
- Y1: value 25Mhz -> X32K768S301; footprint footprints:LFXTAL-25MHz -> Crystal:Crystal_SMD_3215-2Pin_3.2x1.5mm
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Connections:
- C10 pad 1: Net-(U1-SS) -> /power/SENSE_IN-
- C11 pad 1: Net-(U1-COMP) -> /power/SENSE_IN-
- C12 pad 1: Net-(C12-Pad1) -> /power/SENSE_IN-
- C13 pad 1: /power/SENSE_IN+ -> /power/SENSE_IN-
- C13 pad 2: Net-(U1-FB) -> GND
- C14 pad 1: /bmc/+5v -> Net-(U2-SS)
- C15 pad 1: /bmc/+5v -> Net-(U1-BST)
- C15 pad 2: GND -> Net-(U1-SW)
- C16 pad 1: /bmc/+5v -> Net-(U2-COMP)
- C17 pad 1: /bmc/+5v -> Net-(C17-Pad1)
- C18 pad 1: /bmc/+5v -> /bmc/+5v_BMC
- C19 pad 1: Net-(U2-IN+) -> /bmc/+5v_BMC
- C19 pad 2: Net-(U2-IN-) -> GND
- C2 pad 1: Net-(D1-K) -> /power/SENSE_IN+
- C20 pad 1: /bmc/3.3v -> /power/+5v_HOST
- C20 pad 2: GND -> Net-(U2-FB)
- C21 pad 1: /bmc/3.3v -> /bmc/+5v_BMC
- C22 pad 1: /bmc/PHY_DVDDL -> /bmc/+5v_BMC
- C23 pad 1: /bmc/PHY_DVDDL -> /power/+5v_HOST
- C24 pad 1: /bmc/PHY_DVDDL -> /bmc/+5v_BMC
- C25 pad 1: /bmc/PHY_DVDDL -> /power/+5v_HOST
- C26 pad 1: /bmc/PHY_AVDDL_PLL -> /power/+5v_HOST
- C27 pad 1: /bmc/PHY_DVDDL -> /power/+5v_HOST
- C28 pad 1: Net-(C28-Pad1) -> /power/+5v_HOST
- C29 pad 1: /bmc/PHY_AVDDL -> Net-(U4-IN+)
- C29 pad 2: GND -> Net-(U4-IN-)
- C3 pad 1: Net-(D1-K) -> /power/SENSE_IN+
- C30 pad 1: /bmc/PHY_AVDDL_PLL -> /bmc/3.3v_BMC
- C31 pad 1: /bmc/PHY_DVDDL -> /bmc/3.3v_BMC
- C32 pad 1: Net-(C32-Pad1) -> GND
- C32 pad 2: GND -> /cm4/+BATT
- C33 pad 1: /bmc/PHY_AVDDL -> /bmc/+5v_BMC
- C34 pad 1: /bmc/PHY_AVDDL_PLL -> /bmc/+5V_OTG
- C35 pad 1: /bmc/PHY_DVDDL -> /bmc/+5V_OTG
- C36 pad 1: /bmc/PHY_AVDDL -> /bmc/+5V_OTG
- C37 pad 1: /bmc/PHY_AVDDL_PLL -> /bmc/3.3v_BMC
- C38 pad 1: /bmc/PHY_DVDDL -> /bmc/+5V_OTG
- C39 pad 1: /bmc/PHY_AVDDL -> /bmc/+5V_OTG
- C4 pad 1: Net-(D1-K) -> /power/SENSE_IN-
- C40 pad 1: /bmc/PHY_AVDDL -> /bmc/PHY_DVDDL
- C41 pad 1: /bmc/PHY_RESET_N -> /bmc/PHY_DVDDL
- C42 pad 1: /bmc/PHY_AVDDH -> /bmc/PHY_DVDDL
- C43 pad 1: /bmc/1V2 -> /bmc/PHY_DVDDL
- C44 pad 1: /bmc/PHY_DVDDH -> /bmc/PHY_AVDDL_PLL
- C45 pad 1: /bmc/PHY_AVDDH -> /bmc/PHY_DVDDL
- C46 pad 1: /bmc/1V2 -> Net-(C46-Pad1)
- C47 pad 1: /bmc/PHY_DVDDH -> /bmc/PHY_AVDDL
- C48 pad 1: /bmc/PHY_AVDDH -> /bmc/PHY_AVDDL_PLL
- C49 pad 1: /bmc/PHY_DVDDH -> /bmc/PHY_DVDDL
- C5 pad 1: Net-(D1-K) -> /power/SENSE_IN-
- C50 pad 1: /bmc/PHY_AVDDH -> Net-(C50-Pad1)
- C51 pad 1: /bmc/PHY_DVDDH -> /bmc/PHY_AVDDL
- C52 pad 1: /bmc/PHY_AVDDH -> /bmc/PHY_AVDDL_PLL
- C53 pad 1: /bmc/PHY_DVDDH -> /bmc/PHY_DVDDL
- C54 pad 1: /bmc/PHY_DVDDH -> /bmc/PHY_AVDDL
- C55 pad 1: GND -> /bmc/PHY_AVDDL_PLL
- C55 pad 2: Net-(U6-XI) -> GND
- C56 pad 1: Net-(U6-XO) -> /bmc/PHY_DVDDL
- C57 pad 1: /bmc/+5v -> /bmc/PHY_AVDDL
- C58 pad 1: /bmc/+5v -> /bmc/PHY_AVDDL
- C59 pad 1: /bmc/+5v -> /bmc/PHY_RESET_N
- C6 pad 1: Net-(D1-K) -> /power/SENSE_IN-
- C60 pad 1: /bmc/+5v -> /bmc/PHY_AVDDH
- C61 pad 1: /cm4/HDMI_5v -> /bmc/1V2
- C62 pad 1: /cm4/VBUS -> /bmc/PHY_DVDDH
- C63 pad 1: /cm4/VBUS -> /bmc/PHY_AVDDH
- C64 pad 1: /cm4/VBUS -> /bmc/1V2
- C65 pad 1: /cm4/+3V3 PCIe -> /bmc/PHY_DVDDH
- C66 pad 1: /cm4/VBUS -> /bmc/PHY_AVDDH
- C67 pad 1: /cm4/+3V3 PCIe -> /bmc/PHY_DVDDH
- C68 pad 1: /cm4/VBUS -> /bmc/PHY_AVDDH
- C69 pad 1: /cm4/+3V3 PCIe -> /bmc/PHY_DVDDH
- C7 pad 1: Net-(D1-K) -> /power/SENSE_IN-
- C70 pad 1: /cm4/XTALIN -> /bmc/PHY_AVDDH
- C71 pad 1: /cm4/XTALOUT -> /bmc/PHY_DVDDH
- C72 pad 1: /cm4/+3.3v -> /bmc/PHY_DVDDH
- C73 pad 1: /cm4/+3.3v -> GND
- C73 pad 2: GND -> Net-(U12-XI)
- C74 pad 1: /cm4/+3.3v -> Net-(U12-XO)
- C75 pad 1: /cm4/+3.3v -> /cm4/+5v_HOST
- C76 pad 1: /cm4/+3.3v -> /cm4/+5v_HOST
- C77 pad 1: /cm4/+3.3v -> /cm4/+5v_HOST
- C78 pad 1: /cm4/+3.3v -> /cm4/+5v_HOST
- C79 pad 1: /cm4/+3.3v -> /cm4/HDMI_5v
- C8 pad 1: Net-(D1-K) -> /power/SENSE_IN-
- C80 pad 1: /cm4/+3V3 PCIe -> /cm4/VBUS
- C81 pad 1: /cm4/+3V3 PCIe -> /cm4/VBUS
- C82 pad 1: /cm4/+3V3 PCIe -> /cm4/VBUS
- C84 pad 1: /cm4/+3V3 PCIe -> /cm4/VBUS
- C86 pad 1: Net-(C86-Pad1) -> /cm4/VBUS
- C87 pad 1: Net-(C86-Pad1) -> /cm4/+3V3 PCIe
- C9 pad 1: Net-(D1-K) -> /power/SENSE_IN-
- D1 pad 1: Net-(D1-K) -> /power/SENSE_IN+
- D2 pad 1: /bmc/PHY_DVDDH -> Net-(BT1-+)
- D2 pad 2: /bmc/PHY_RESET_N -> /bmc/3.3v_BMC
- D3 pad 1: /bmc/RESET_OUT_N -> Net-(D3-K)
- D3 pad 2: /bmc/PHY_RESET_N -> /bmc/3.3v_BMC
- D4 pad 2: /cm4/+3.3v -> /bmc/+3.3v
- D5 pad 1: Net-(D5-K) -> /bmc/PHY_DVDDH
- D5 pad 2: /cm4/+3.3v -> /bmc/PHY_RESET_N
- FB1 pad 1: /bmc/1V2 -> GND
- FB1 pad 2: /bmc/PHY_DVDDL -> Net-(J4-GND)
- FB2 pad 2: /bmc/PHY_AVDDL_PLL -> /bmc/PHY_DVDDL
- FB3 pad 2: /bmc/PHY_AVDDL -> /bmc/PHY_AVDDL_PLL
- FB4 pad 1: GND -> /bmc/1V2
- FB4 pad 2: Net-(FB4-Pad2) -> /bmc/PHY_AVDDL
- FB5 pad 1: /bmc/PHY_AVDDH -> GND
- FB5 pad 2: /bmc/3.3v -> Net-(FB5-Pad2)
- FB6 pad 1: /bmc/PHY_DVDDH -> /bmc/PHY_AVDDH
- FB6 pad 2: /bmc/3.3v -> /bmc/3.3v_BMC
- FB7 pad 1: Net-(FB7-Pad1) -> /bmc/PHY_DVDDH
- FB7 pad 2: GND -> /bmc/3.3v_BMC
- J2 pad 1: /bmc/TXRXA_P -> Net-(J2-Pin_1)
- J2 pad 2: /bmc/TXRXA_N -> /bmc/3.3v_BMC
- J3 pad 1: /cm4/VBUS -> GND
- J3 pad 2: /cm4/VBUS -> /bmc/BMC_DEBUG_TX
- J3 pad 3: /cm4/HD3_N -> /bmc/BMC_DEBUG_RX
- J4 pad 1: /cm4/CM4_GPIO/TRD0_P -> /bmc/+5V_OTG
- J4 pad 2: /cm4/CM4_GPIO/TRD0_N -> /bmc/BMC_USB_OTG_N
- J4 pad 3: /cm4/CM4_GPIO/TRD1_P -> /bmc/BMC_USB_OTG_P
- J4 pad 4: /cm4/CM4_GPIO/TRD1_N -> /bmc/BMC_USB_IDDET
- J4 pad 5: Net-(C35-Pad1) -> Net-(J4-GND)
- J4 pad 6: Net-(C35-Pad1) -> Net-(J4-GND)
- J5 pad 1: GND -> /bmc/TXRXA_P
- J5 pad 10: unconnected-(J5-DAS/~DSS~/~LED1-Pad10) -> /bmc/TXRXD_N
- J5 pad 11: unconnected-(J5-PETn3-Pad11) -> /bmc/PHY_DVDDH
- J5 pad 12: /cm4/+3V3 PCIe -> Net-(J5-LED2-)
- J5 pad 13: unconnected-(J5-PETp3-Pad13) -> /bmc/PHY_DVDDH
- J5 pad 14: /cm4/+3V3 PCIe -> Net-(J5-LED1-)
- J5 pad 2: /cm4/+3V3 PCIe -> /bmc/TXRXA_N
- J5 pad 3: GND -> /bmc/TXRXB_P
- J5 pad 4: /cm4/+3V3 PCIe -> /bmc/TXRXB_N
- J5 pad 5: unconnected-(J5-PERn3-Pad5) -> Net-(C46-Pad1)
- J5 pad 6: unconnected-(J5-NC-Pad6) -> Net-(C50-Pad1)
- J5 pad 7: unconnected-(J5-PERp3-Pad7) -> /bmc/TXRXC_P
- J5 pad 8: unconnected-(J5-NC-Pad8) -> /bmc/TXRXC_N
- J5 pad 9: GND -> /bmc/TXRXD_P
- J6 pad 1: /cm4/TRD0_P -> /cm4/VBUS
- J6 pad 10: /cm4/TRD3_N -> unconnected-(J6-Pin_10-Pad10)
- J6 pad 2: /cm4/TRD0_N -> /cm4/VBUS
- J6 pad 3: /cm4/TRD1_P -> /cm4/HD3_N
- J6 pad 4: /cm4/TRD1_N -> /cm4/HD4_N
- J6 pad 5: Net-(C86-Pad1) -> /cm4/HD3_P
- J6 pad 6: Net-(C86-Pad1) -> /cm4/HD4_P
- J6 pad 7: /cm4/TRD2_P -> GND
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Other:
- board size 5.8 x 5.9 mm -> 5.9 x 5.8 mm
